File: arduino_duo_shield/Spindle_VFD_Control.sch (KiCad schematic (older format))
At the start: 25 parts, among them K2 JQC-3F, K3 JQC-3F, Q3 2N7000, Q4 BS250, Q5 2N7000, Q6 2N7000, U7 PC817, U8 PC817, U9 PC817

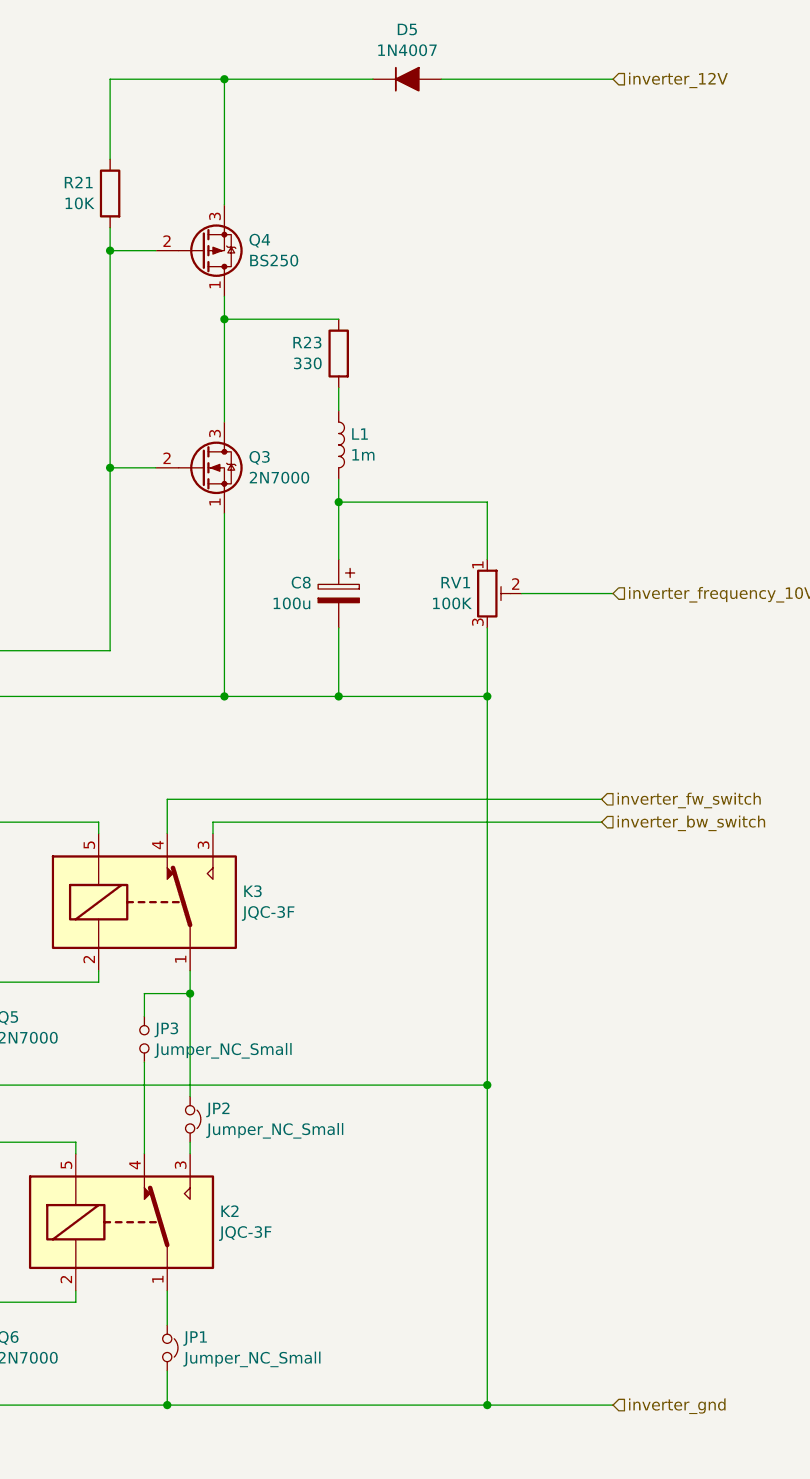
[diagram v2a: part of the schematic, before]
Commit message: Route all paths
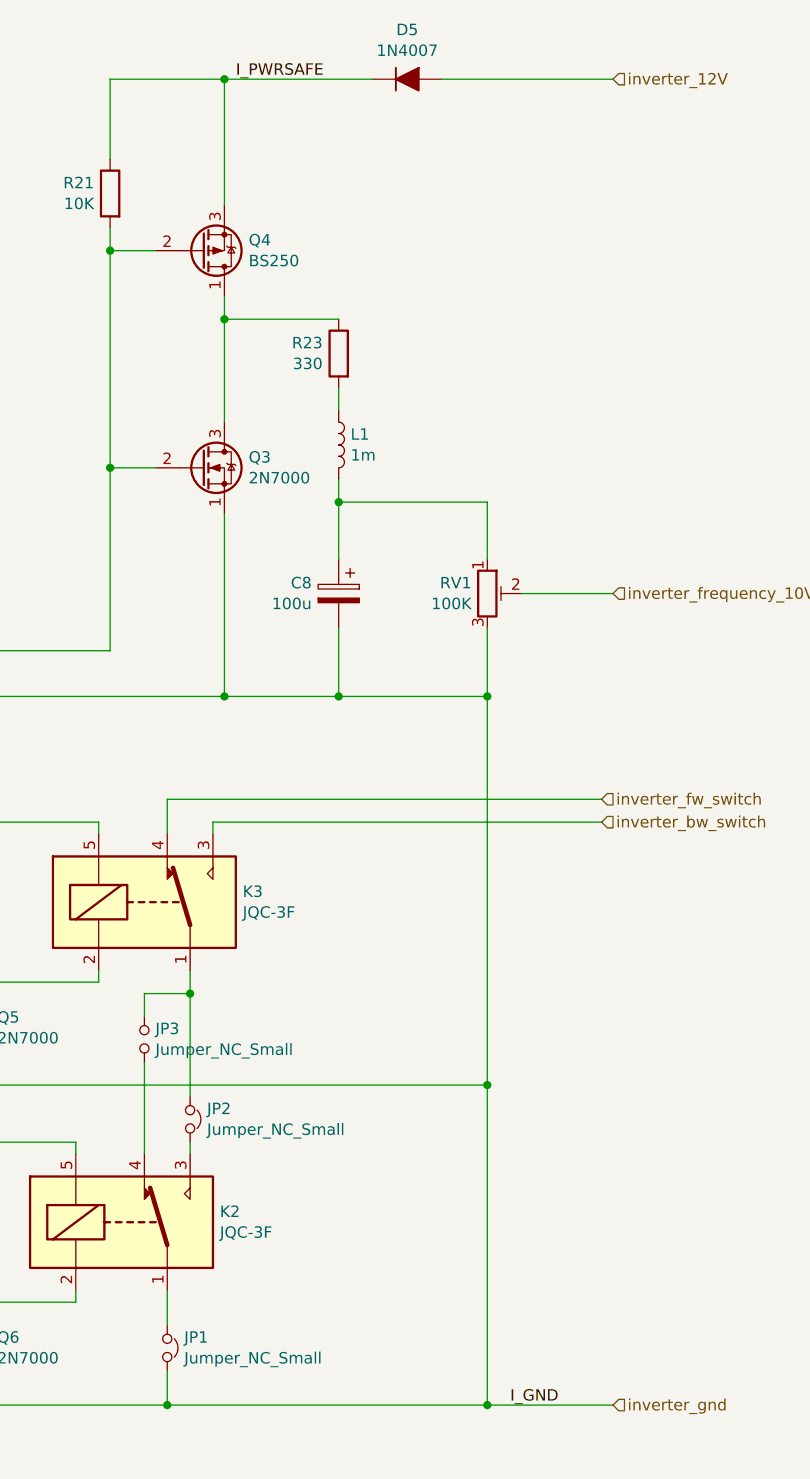
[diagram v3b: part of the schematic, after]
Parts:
- C8: footprint Capacitor_THT:C_Disc_D3.0mm_W2.0mm_P2.50mm -> Capacitor_THT:CP_Radial_D8.0mm_P3.50mm
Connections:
- net I_PWRSAFE: now reaches D5.1 (K), Q4.3 (S), R21.1
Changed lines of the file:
@@
 $Descr A4 11693 8268
 encoding utf-8
-Sheet 5 5
+Sheet 4 4
 Title ""
 Date ""
@@
 F 0 "C8" H 5168 3096 50  0000 L CNN
 F 1 "100u" H 5168 3005 50  0000 L CNN
-F 2 "Capacitor_THT:C_Disc_D3.0mm_W2.0mm_P2.50mm" H 5088 2900 50  0001 C CNN
+F 2 "Capacitor_THT:CP_Radial_D8.0mm_P3.50mm" H 5088 2900 50  0001 C CNN
 F 3 "~" H 5050 3050 50  0001 C CNN
 	1    5050 3050
@@
 	0    1    1    0
 $EndComp
+Text Label 4600 800  0    50   ~ 0
+I_PWRSAFE
+Text Label 5800 6600 0    50   ~ 0
+I_GND
 $EndSCHEMATC

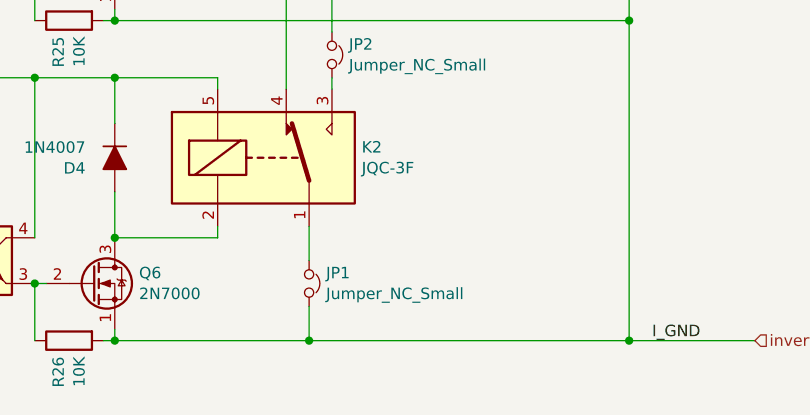
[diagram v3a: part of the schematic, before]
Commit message: Add silk screen labels and version number
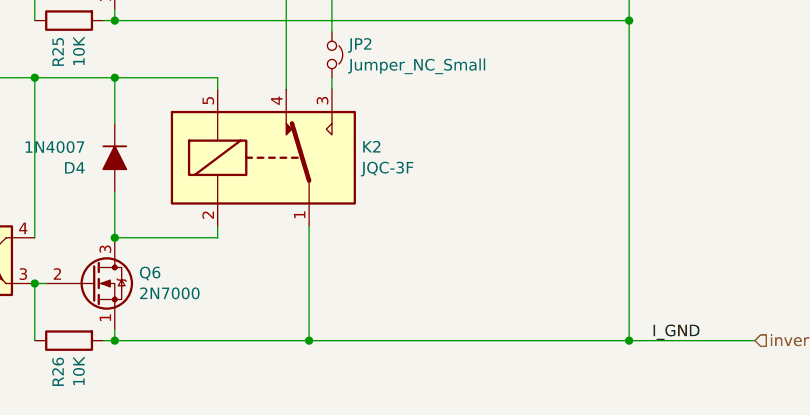
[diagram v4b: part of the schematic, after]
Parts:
- removed JP1: Jumper_NC_Small, Connector_PinHeader_2.54mm:PinHeader_1x02_P2.54mm_Vertical, symbol Device:Jumper_NC_Small
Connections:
- net inverter_gnd: now also K2.1
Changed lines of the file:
@@
 Connection ~ 4050 2500
-Wire Wire Line
-	4300 6100 4300 6250
 Wire Wire Line
 	4300 6600 3450 6600
@@
 Wire Wire Line
 	4400 5450 4400 5500
-$Comp
-L Device:Jumper_NC_Small JP1
-U 1 1 5E3EDC9D
-P 4300 6350
-F 0 "JP1" V 4254 6424 50  0000 L CNN
-F 1 "Jumper_NC_Small" V 4345 6424 50  0000 L CNN
-F 2 "Connector_PinHeader_2.54mm:PinHeader_1x02_P2.54mm_Vertical" H 4300 6350 50  0001 C CNN
-F 3 "~" H 4300 6350 50  0001 C CNN
-	1    4300 6350
-	0    1    1    0
-$EndComp
-Wire Wire Line
-	4300 6450 4300 6600
 Wire Wire Line
 	4200 4800 4400 4800
@@
 Text Label 5800 6600 0    50   ~ 0
 I_GND
+Wire Wire Line
+	4300 6100 4300 6600
 $EndSCHEMATC

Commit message: Generate gerber files for 1.0-alpha-1
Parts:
- added D1: LED, LED_THT:LED_D3.0mm, symbol Device:LED
- R21: value 10K -> 1K5
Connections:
- net I_PWRSAFE: now also D1.2 (A); no longer R21.1
- new net: D1.1 (K), R21.1
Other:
- moved on the sheet: R21
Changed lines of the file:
@@
 L Device:R R?
 U 1 1 5DD63534
-P 4050 1300
+P 4050 1350
 AR Path="/5D7DFDC0/5DD63534" Ref="R?"  Part="1"
 AR Path="/5DD17641/5DD63534" Ref="R21"  Part="1"
-F 0 "R21" H 4120 1346 50  0000 L CNN
-F 1 "10K" H 4120 1255 50  0000 L CNN
-F 2 "Resistor_THT:R_Axial_DIN0207_L6.3mm_D2.5mm_P7.62mm_Horizontal" V 3980 1300 50  0001 C CNN
-F 3 "~" H 4050 1300 50  0001 C CNN
-	1    4050 1300
+F 0 "R21" H 4120 1396 50  0000 L CNN
+F 1 "1K5" H 4120 1305 50  0000 L CNN
+F 2 "Resistor_THT:R_Axial_DIN0207_L6.3mm_D2.5mm_P7.62mm_Horizontal" V 3980 1350 50  0001 C CNN
+F 3 "~" H 4050 1350 50  0001 C CNN
+	1    4050 1350
 	-1   0    0    -1
 $EndComp
@@
 $EndComp
 Wire Wire Line
-	4050 1450 4050 1550
-Wire Wire Line
 	4250 2500 4050 2500
 Wire Wire Line
@@
 Wire Wire Line
 	4050 1550 4250 1550
-Connection ~ 4050 1550
 Wire Wire Line
 	4050 1550 4050 2500
@@
 	4550 800  4050 800
 Wire Wire Line
-	4050 800  4050 1150
+	4050 800  4050 850
 Wire Wire Line
 	5050 2150 5050 2250
@@
 Wire Wire Line
 	4300 6100 4300 6600
+Wire Wire Line
+	4050 1500 4050 1550
+Connection ~ 4050 1550
+Wire Wire Line
+	4050 1150 4050 1200
+$Comp
+L Device:LED D1
+U 1 1 5E0AD300
+P 4050 1000
+F 0 "D1" V 4089 883 50  0000 R CNN
+F 1 "LED" V 3998 883 50  0000 R CNN
+F 2 "LED_THT:LED_D3.0mm" H 4050 1000 50  0001 C CNN
+F 3 "~" H 4050 1000 50  0001 C CNN
+	1    4050 1000
+	0    -1   -1   0
+$EndComp
 $EndSCHEMATC
